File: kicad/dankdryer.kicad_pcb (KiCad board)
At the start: 2 copper layers, 100 x 75 mm, 39 parts, among them J1 Barreljack, J2 upper fan, J3 lower fan, J4 heater, J5 Screw_Terminal_01x04, J7 5kg load cell, J8 motor, J9 Conn_01x04, Q1 BT136S-800E, Q2 SSM3K127TU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

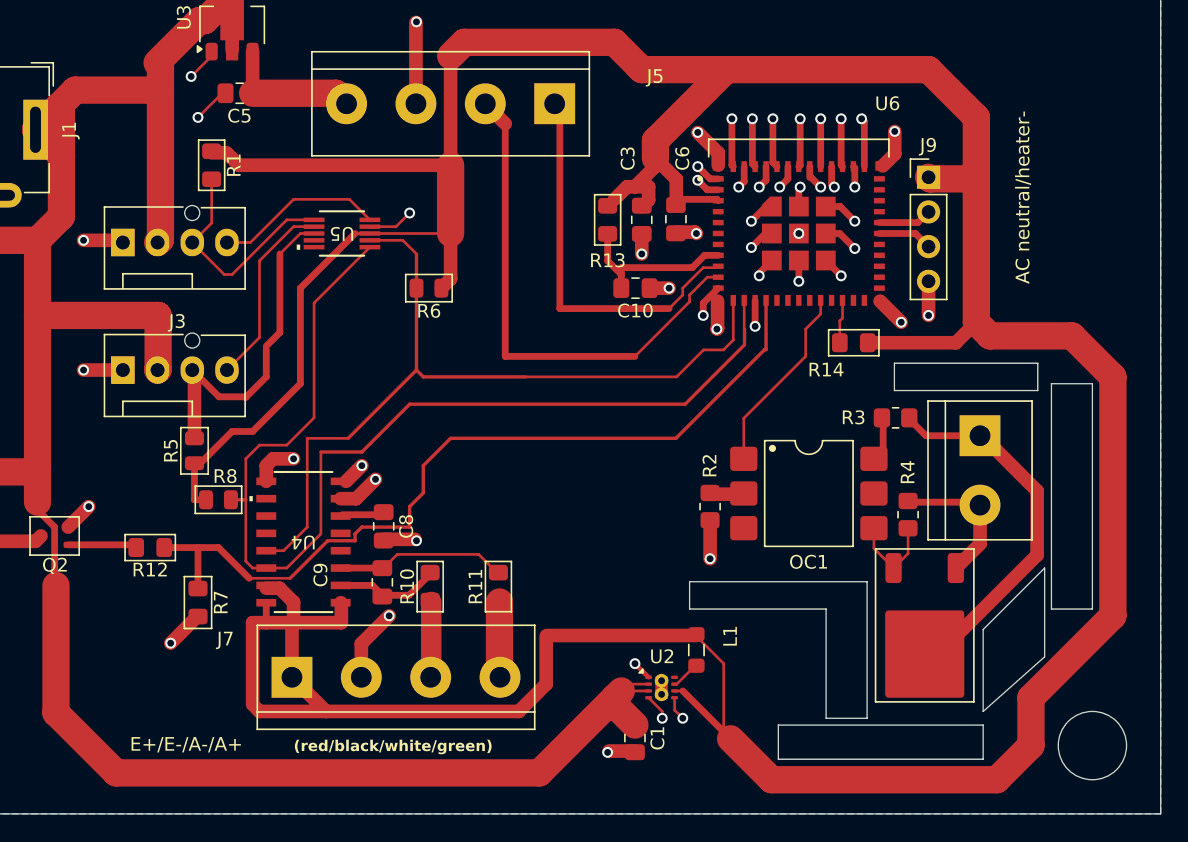
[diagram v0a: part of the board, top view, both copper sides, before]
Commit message: kicad: use hand-solderable 0805s
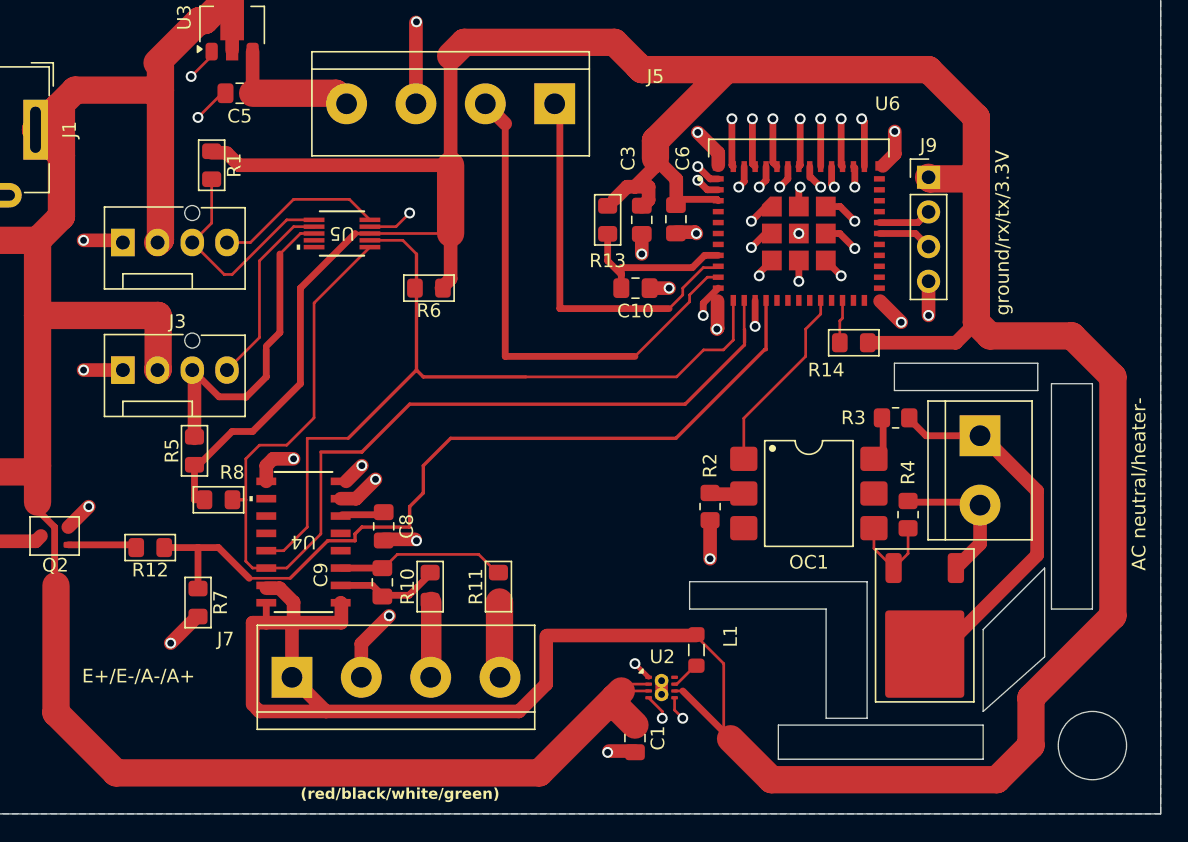
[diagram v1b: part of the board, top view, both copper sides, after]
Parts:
- R5, R6, R8: footprint PCM_Resistor_SMD_AKL:R_0805_2012Metric -> PCM_Resistor_SMD_AKL:R_0805_2012Metric_Pad1.15x1.40mm_HandSolder
- R7: footprint PCM_Resistor_SMD_AKL:R_0805_2012Metric_Pad1.15x1.40mm -> PCM_Resistor_SMD_AKL:R_0805_2012Metric_Pad1.15x1.40mm_HandSolder
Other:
- board text added: "ground/rx/tx/3.3V"

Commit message: fix resistor input to triac
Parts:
- R2: value 330 -> 660
- moved R2 10.5 mm to (122.5, 93.5), turned to 90 degrees
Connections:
- OC1 pad 1: /SSRControl -> Net-(OC1-A)
- OC1 pad 2: Net-(OC1-Pad2) -> GND
- R2 pad 1: Net-(OC1-Pad2) -> Net-(OC1-A)
- R2 pad 2: GND -> /SSRControl
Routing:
- net /SSRControl: track 13.9 -> 6.18 mm
- net Net-(OC1-A): track 0.00 -> 5.76 mm
- net Net-(OC1-Pad2): track 2.65 -> 0.00 mm
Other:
- board text added: "HallD/ThermA/ground/5V"
- board text removed: "5VDC/GND/ThermA/HallD"
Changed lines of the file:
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@@
 			(sketchpadsonfab no)
 			(subtractmaskfromsilk no)
-			(outputformat 4)
+			(outputformat 1)
 			(mirror no)
 			(drillshape 0)
@@
 	(net 15 "/A-")
 	(net 16 "Net-(U2-SW)")
-	(net 17 "Net-(Q1-G)")
+	(net 17 "Net-(OC1-MT2)")
 	(net 18 "unconnected-(OC1-NC-Pad5)")
 	(net 19 "unconnected-(OC1-NC-Pad3)")
-	(net 20 "Net-(OC1-Pad6)")
-	(net 21 "Net-(OC1-Pad2)")
+	(net 20 "Net-(OC1-A)")
+	(net 21 "Net-(OC1-MT1)")
 	(net 22 "Net-(Q2-G)")
 	(net 23 "unconnected-(U6-NC-Pad33)")
@@
 			(layers "F.Cu" "F.Paste" "F.Mask")
 			(roundrect_rratio 0.208333)
-			(net 17 "Net-(Q1-G)")
+			(net 21 "Net-(OC1-MT1)")
 			(pintype "passive")
 		)
@@
 	(footprint "Resistor_SMD:R_0805_2012Metric_Pad1.20x1.40mm_HandSolder"
 		(layer "F.Cu")
-		(at 117 102.5 -90)
+		(at 122.5 93.5 90)
 		(descr "Resistor SMD 0805 (2012 Metric), square (rectangular) end terminal, IPC_7351 nominal with elongated pad for handsoldering. (Body size source: IPC-SM-782 page 72, https://www.pcb-3d.com/wordpress/wp-content/uploads/ipc-sm-782a_amendment_1_and_2.pdf), generated with kicad-footprint-generator")
 		(tags "resistor handsolder")
 		(property "Reference" "R2"
-			(at -3 0 -90)
+			(at -3 0 90)
 			(layer "F.SilkS")
 			(effects
@@
 			)
 		)
-		(property "Value" "330"
-			(at 0 1.65 -90)
+		(property "Value" "660"
+			(at 0 1.65 90)
 			(layer "F.Fab")
 			(effects
@@
 		)
 		(property "Footprint" "Resistor_SMD:R_0805_2012Metric_Pad1.20x1.40mm_HandSolder"
-			(at 0 0 -90)
+			(at 0 0 90)
 			(unlocked yes)
 			(layer "F.Fab")
@@
 		)
 		(property "Datasheet" ""
-			(at 0 0 -90)
+			(at 0 0 90)
 			(unlocked yes)
 			(layer "F.Fab")
@@
 		)
 		(property "Description" "Resistor"
-			(at 0 0 -90)
+			(at 0 0 90)
 			(unlocked yes)
 			(layer "F.Fab")
@@
 		(attr smd)
 		(fp_line
-			(start -0.227064 0.735)
-			(end 0.227064 0.735)
+			(start -0.227064 -0.735)
+			(end 0.227064 -0.735)
 			(stroke
 				(width 0.12)
@@
 		)
 		(fp_line
-			(start -0.227064 -0.735)
-			(end 0.227064 -0.735)
+			(start -0.227064 0.735)
+			(end 0.227064 0.735)
 			(stroke
 				(width 0.12)
@@
 		)
 		(fp_line
-			(start -1.85 0.95)
-			(end -1.85 -0.95)
+			(start 1.85 -0.95)
+			(end 1.85 0.95)
 			(stroke
 				(width 0.05)
@@
 		)
 		(fp_line
-			(start 1.85 0.95)
-			(end -1.85 0.95)
+			(start -1.85 -0.95)
+			(end 1.85 -0.95)
 			(stroke
 				(width 0.05)
@@
 		)
 		(fp_line
-			(start -1.85 -0.95)
-			(end 1.85 -0.95)
+			(start 1.85 0.95)
+			(end -1.85 0.95)
 			(stroke
 				(width 0.05)
@@
 		)
 		(fp_line
-			(start 1.85 -0.95)
-			(end 1.85 0.95)
+			(start -1.85 0.95)
+			(end -1.85 -0.95)
 			(stroke
 				(width 0.05)
@@
 		)
 		(fp_line
-			(start -1 0.625)
-			(end -1 -0.625)
+			(start 1 -0.625)
+			(end 1 0.625)
 			(stroke
 				(width 0.1)
@@
 		)
 		(fp_line
-			(start 1 0.625)
-			(end -1 0.625)
+			(start -1 -0.625)
+			(end 1 -0.625)
 			(stroke
 				(width 0.1)
@@
 		)
 		(fp_line
-			(start -1 -0.625)
-			(end 1 -0.625)
+			(start 1 0.625)
+			(end -1 0.625)
 			(stroke
 				(width 0.1)
@@
 		)
 		(fp_line
-			(start 1 -0.625)
-			(end 1 0.625)
+			(start -1 0.625)
+			(end -1 -0.625)
 			(stroke
 				(width 0.1)
@@
 		)
 		(fp_text user "${REFERENCE}"
-			(at 0 0 -90)
+			(at 0 0 90)
 			(layer "F.Fab")
 			(effects
@@
 		)
 		(pad "1" smd roundrect
-			(at -1 0 270)
+			(at -1 0 90)
 			(size 1.2 1.4)
 			(layers "F.Cu" "F.Paste" "F.Mask")
 			(roundrect_rratio 0.208333)
-			(net 21 "Net-(OC1-Pad2)")
+			(net 20 "Net-(OC1-A)")
 			(pintype "passive")
 		)
 		(pad "2" smd roundrect
-			(at 1 0 270)
+			(at 1 0 90)
 			(size 1.2 1.4)
 			(layers "F.Cu" "F.Paste" "F.Mask")
 			(roundrect_rratio 0.208333)
-			(net 1 "GND")
+			(net 48 "/SSRControl")
 			(pintype "passive")
 		)
@@
 		(tags "SOT-89-3")
 		(property "Reference" "U3"
-			(at 0.55 -3.5 90)
+			(at 2.228125 -4.5 90)
 			(layer "F.SilkS")
 			(effects
@@
 		(tags "terminal block bornier4")
 		(property "Reference" "J5"
-			(at -7.38 2 0)
+			(at -3.88 0 0)
 			(layer "F.SilkS")
 			(effects
@@
 		(tags "pin header 4-pin CPU fan")
 		(property "Reference" "J3"
-			(at 4 -3.55 0)
+			(at 4.5 -4 0)
 			(layer "F.SilkS")
 			(effects
@@
 			(layers "F.Cu" "F.Paste" "F.Mask")
 			(roundrect_rratio 0.208333)
-			(net 20 "Net-(OC1-Pad6)")
+			(net 17 "Net-(OC1-MT2)")
 			(pintype "passive")
 		)
@@
 		(tags "capacitor handsolder")
 		(property "Reference" "C10"
-			(at 0 -1.68 0)
+			(at 1.0375 -3 0)
 			(layer "F.SilkS")
 			(effects
@@
 			(layers "F.Cu" "F.Paste" "F.Mask")
 			(roundrect_rratio 0.1404494382)
-			(net 48 "/SSRControl")
+			(net 20 "Net-(OC1-A)")
+			(pinfunction "A")
 			(pintype "passive")
 		)
@@
 			(layers "F.Cu" "F.Paste" "F.Mask")
 			(roundrect_rratio 0.1404494382)
-			(net 21 "Net-(OC1-Pad2)")
+			(net 1 "GND")
+			(pinfunction "C")
 			(pintype "passive")
 		)
@@
 			(layers "F.Cu" "F.Paste" "F.Mask")
 			(roundrect_rratio 0.1404494382)
-			(net 17 "Net-(Q1-G)")
+			(net 21 "Net-(OC1-MT1)")
+			(pinfunction "MT1")
 			(pintype "passive")
 		)
@@
 			(layers "F.Cu" "F.Paste" "F.Mask")
 			(roundrect_rratio 0.1404494382)
-			(net 20 "Net-(OC1-Pad6)")
+			(net 17 "Net-(OC1-MT2)")
+			(pinfunction "MT2")
 			(pintype "passive")
 		)
@@
 			(layers "F.Cu" "F.Paste" "F.Mask")
 			(roundrect_rratio 0.2083333333)
-			(net 17 "Net-(Q1-G)")
+			(net 21 "Net-(OC1-MT1)")
 			(pinfunction "G")
 			(pintype "input")
@@
 		(tags "resistor handsolder")
 		(property "Reference" "R1"
-			(at 0 -1.65 -90)
+			(at 1.5 -2 -90)
 			(layer "F.SilkS")
 			(effects
@@
 		)
 	)
-	(gr_text "5VDC/GND/ThermA/HallD\n"
-		(at 89 65 0)
+	(gr_text "HallD/ThermA/ground/5V\n"
+		(at 107.5 65 180)
 		(layer "F.SilkS")
 		(effects
@@
 	)
 	(segment
+		(start 117.04 101.54)
+		(end 117 101.5)
+		(width 0.2)
+		(layer "F.Cu")
+		(net 1)
+	)
+	(segment
 		(start 118.6 74.1)
 		(end 118.6 77.5)
@@
 	)
 	(segment
-		(start 117 103.68125)
-		(end 117 106.31875)
-		(width 1)
-		(layer "F.Cu")
-		(net 1)
-	)
-	(segment
 		(start 133 86)
 		(end 133 88.5)
@@
 	)
 	(segment
+		(start 119.47 101.54)
+		(end 117.04 101.54)
+		(width 1)
+		(layer "F.Cu")
+		(net 1)
+	)
+	(segment
 		(start 111.5 120.4)
 		(end 109.6 120.4)
@@
 	)
 	(via
-		(at 117 106.31875)
+		(at 119.1 79.1)
 		(size 0.8)
 		(drill 0.5)
 		(layers "F.Cu" "B.Cu")
-		(free yes)
 		(net 1)
 	)
 	(via
-		(at 119.1 79.1)
+		(at 126.6 74.1)
 		(size 0.8)
 		(drill 0.5)
@@
 	)
 	(via
-		(at 126.6 74.1)
+		(at 117 101.5)
 		(size 0.8)
 		(drill 0.5)
 		(layers "F.Cu" "B.Cu")
+		(free yes)
 		(net 1)
 	)
@@
 	)
 	(segment
+		(start 129.675 96)
+		(end 129.675 98.325)
+		(width 0.5)
+		(layer "F.Cu")
+		(net 17)
+	)
+	(segment
+		(start 122.5 94.5)
+		(end 119.47 97.53)
+		(width 0.2)
+		(layer "F.Cu")
+		(net 20)
+	)
+	(segment
+		(start 119.47 97.53)
+		(end 119.47 99)
+		(width 0.2)
+		(layer "F.Cu")
+		(net 20)
+	)
+	(segment
 		(start 131.5 104)
 		(end 131.5 105.94)
 		(width 0.2)
 		(layer "F.Cu")
-		(net 17)
+		(net 21)
 	)
 	(segment
@@
 		(width 0.2)
 		(layer "F.Cu")
-		(net 17)
+		(net 21)
 	)
 	(segment
@@
 		(width 0.2)
 		(layer "F.Cu")
-		(net 17)
+		(net 21)
 	)
 	(segment
@@
 		(width 0.2)
 		(layer "F.Cu")
-		(net 17)
-	)
-	(segment
-		(start 129.675 96)
-		(end 129.675 98.325)
-		(width 0.5)
-		(layer "F.Cu")
-		(net 20)
-	)
-	(segment
-		(start 117 101.5875)
-		(end 119.6475 101.5875)
-		(width 1)
-		(layer "F.Cu")
 		(net 21)
 	)
@@
 	)
 	(segment
-		(start 124 89.5)
-		(end 124 91.5)
+		(start 122.5 92.5)
+		(end 125.1 89.9)
 		(width 0.2)
 		(layer "F.Cu")
@@
 	)
 	(segment
-		(start 124 91.5)
-		(end 119.47 96.03)
-		(width 0.2)
-		(layer "F.Cu")
-		(net 48)
-	)
-	(segment
-		(start 125.1 87.4)
-		(end 125.1 88.4)
-		(width 0.2)
-		(layer "F.Cu")
-		(net 48)
-	)
-	(segment
-		(start 125.1 88.4)
-		(end 124 89.5)
-		(width 0.2)
-		(layer "F.Cu")
-		(net 48)
-	)
-	(segment
-		(start 119.47 96.03)
-		(end 119.47 99)
+		(start 125.1 89.9)
+		(end 125.1 87.4)
 		(width 0.2)
 		(layer "F.Cu")

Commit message: move 12V -> 3.3V conversion to lower left
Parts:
- R13: value 10K -> 10k
- R14: value 3.3K -> 3.3k
- R7: value 1.62K -> 1.62k
- moved C1 41.0 mm to (70.5, 121.5)
- moved U2 41.0 mm to (72.5, 117.8)
- moved L1 39.8 mm to (76.3, 116.0), turned to 0 degrees
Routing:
- net +12V: track 165.1 -> 120.1 mm
- net +3.3V: track 302.6 -> 307.1 mm

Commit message: clean up i2c bus
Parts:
- U4: value NAU7802SGI-dank -> NAU7802SGI
- U5: value EMC2302-2-AIZL-TR -> EMC2302
- moved U4 14.1 mm to (100.9, 101.7), turned to 90 degrees
- moved R8 12.6 mm to (91.5, 95.0)
- moved C8 12.1 mm to (104.5, 108.0)
- moved C9 6.02 mm to (99.0, 107.5), turned to 0 degrees
- moved R5 1.55 mm to (80.5, 97.5), turned to 180 degrees
- moved R10 0.50 mm to (96.0, 108.4)
- moved R11 0.50 mm to (102.0, 108.4)
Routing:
- net /SDA: track 79.5 -> 52.1 mm
- net +3.3V: track 307.1 -> 323.7 mm
- net /SCL: track 60.0 -> 45.8 mm
- net Net-(U4-VIN1P): track 12.5 -> 5.28 mm
- net /MotorPin: track 60.9 -> 56.6 mm
- net Net-(U4-VIN1N): track 7.49 -> 5.40 mm
- net GND: track 136.4 -> 135.1 mm
- net Net-(J3-Pin_3): track 24.2 -> 25.0 mm
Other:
- board text added: "5kg load cell (red/black/white/green)"
- board text removed: "(red/black/white/green)"

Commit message: remove bogon copper layer
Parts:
- R2: value 660 -> 620
- U3: value HT7550-1-SOT89 -> HT7550
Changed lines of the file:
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@@
 			(sketchpadsonfab no)
 			(subtractmaskfromsilk no)
-			(outputformat 4)
+			(outputformat 1)
 			(mirror no)
 			(drillshape 0)
@@
 			)
 		)
-		(property "Value" "660"
+		(property "Value" "620"
 			(at 0 2 90)
 			(layer "F.Fab")
@@
 			)
 		)
-		(property "Value" "HT7550-1-SOT89"
-			(at 3.228125 -8 180)
+		(property "Value" "HT7550"
+			(at 3.728125 -4 180)
 			(layer "F.SilkS")
 			(effects
@@
 		(tags "capacitor handsolder")
 		(property "Reference" "C10"
-			(at 1.0375 -3 0)
+			(at 3.5375 0 0)
 			(layer "F.SilkS")
 			(effects
@@
 	)
 	(zone
-		(net 1)
-		(net_name "GND")
-		(layer "B.Cu")
-		(hatch edge 0.5)
-		(priority 1)
-		(connect_pads
-			(clearance 0.5)
-		)
-		(min_thickness 0.25)
-		(filled_areas_thickness no)
-		(fill yes
-			(thermal_gap 0.5)
-			(thermal_bridge_width 0.5)
-		)
-		(polygon
-			(pts
-				(xy 50 50) (xy 50 -50) (xy 125 -50) (xy 125 50)
-			)
-		)
-	)
-	(zone

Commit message: pcb v0.95
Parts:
- OC1: value MOC3063SM -> MOC3063S; footprint PCM_Package_DIP_AKL:SMDIP-6_W9.53mm -> dank:MOC306XS_LTO
- U3: value HT7550 -> HT7550-1-SOT89
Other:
- board text added: "v0.95 2024-12-20 by nick black"
- board text removed: "v0.94 2024-12-19 by nick black"

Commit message: HT7550 is sufficient, thanks
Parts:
- U3: value HT7550-1-SOT89 -> HT7550
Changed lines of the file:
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@@
 			(sketchpadsonfab no)
 			(subtractmaskfromsilk no)
-			(outputformat 4)
+			(outputformat 1)
 			(mirror no)
 			(drillshape 0)
@@
 			)
 		)
-		(property "Value" "HT7550-1-SOT89"
+		(property "Value" "HT7550"
 			(at 3.728125 -4 180)
 			(layer "F.SilkS")

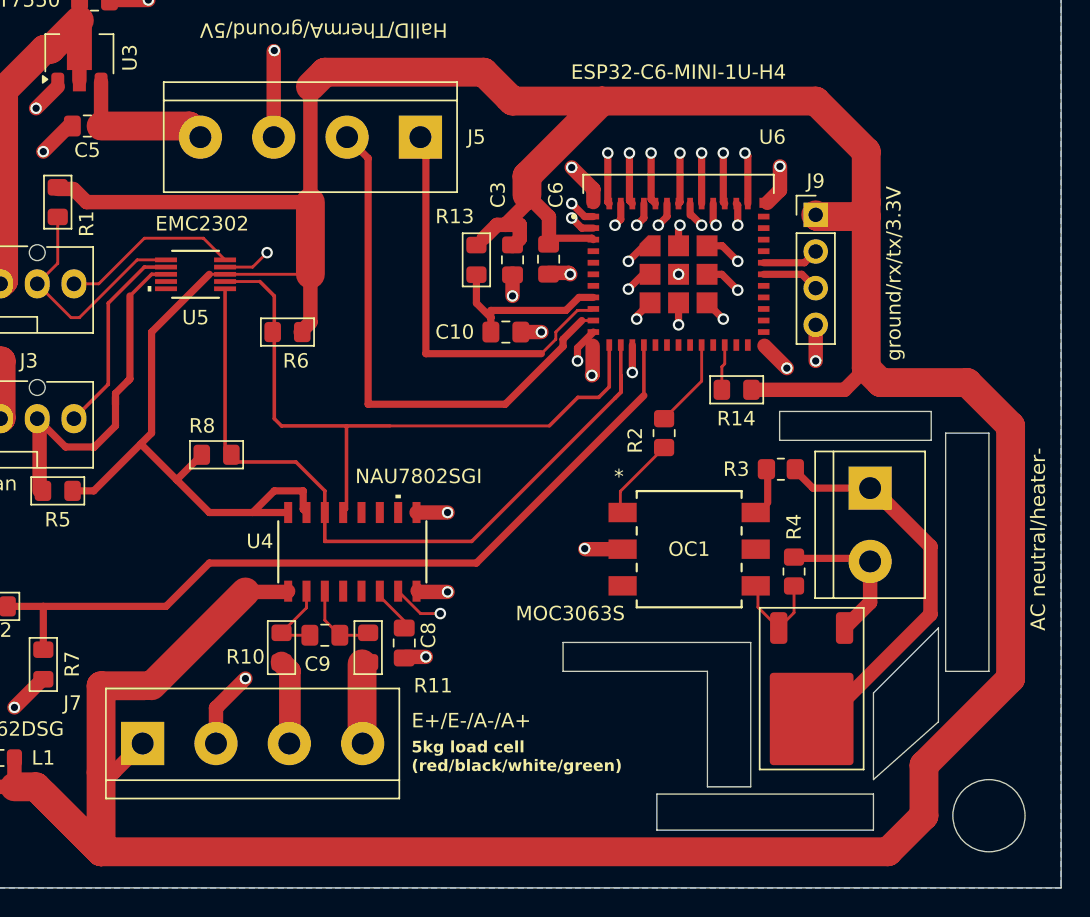
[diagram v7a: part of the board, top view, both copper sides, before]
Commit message: dump app versions in all ota partitions
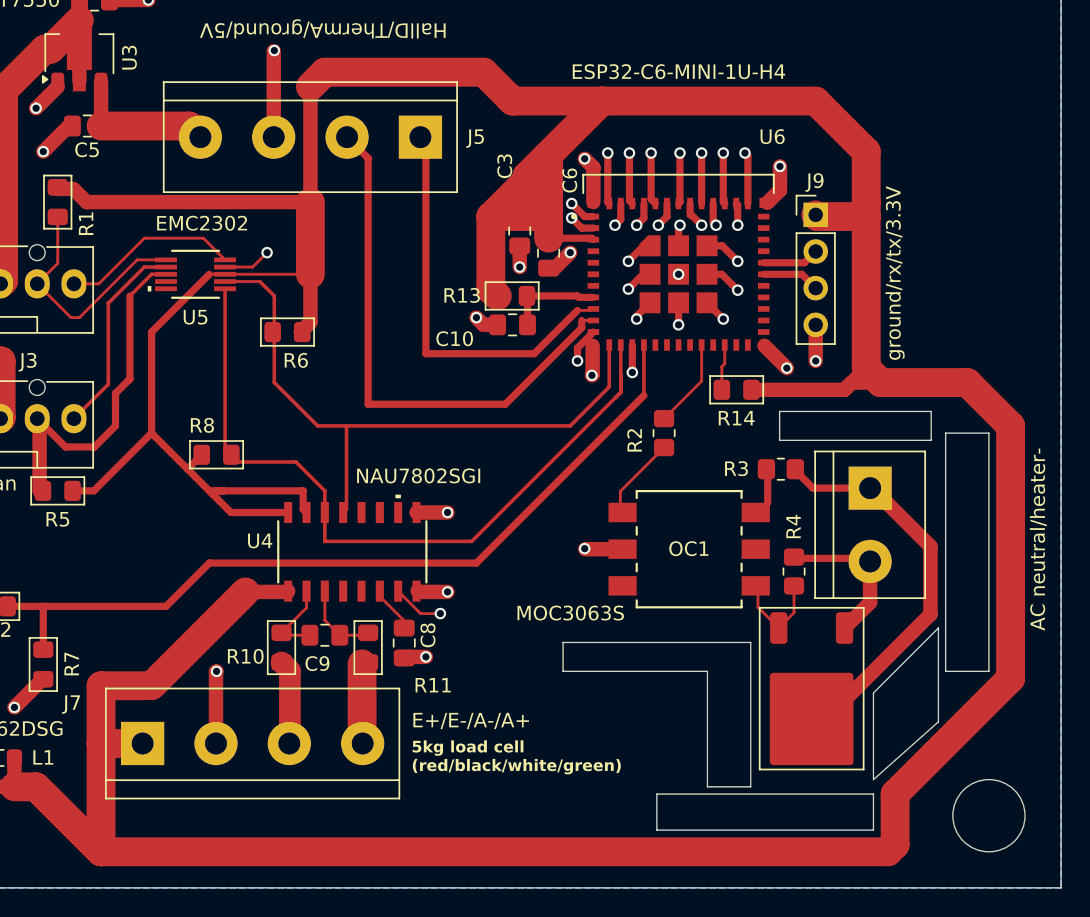
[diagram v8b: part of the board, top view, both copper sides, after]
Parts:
- moved R13 3.52 mm to (112.0, 84.0), turned to 0 degrees
- moved C3 2.06 mm to (112.5, 79.5)
- moved C10 0.68 mm to (112.0, 86.0), turned to 0 degrees
- moved C6 0.41 mm to (114.5, 81.0)
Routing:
- net +3.3V: track 323.7 -> 337.2 mm
- net Net-(U6-EN): track 12.4 -> 6.60 mm
- net /SCL: track 45.8 -> 44.4 mm
